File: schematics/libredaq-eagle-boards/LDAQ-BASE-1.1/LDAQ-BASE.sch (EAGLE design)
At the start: 90 parts, among them J1 4840.2211, J2 M50-3610542, T1 FDN340P, U1 ATSAM3U1CB, U2 LM3671MF-3.3, U3 TS30012-M050QFNR, U4 ISL3175, U5 LMV321, U6 TXB0108PWR, Y1 12M

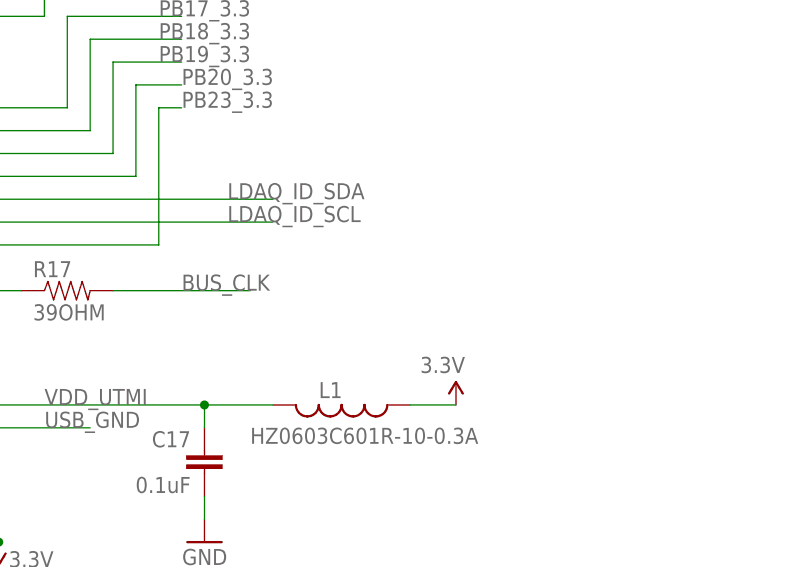
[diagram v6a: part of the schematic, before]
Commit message: Revision with CPLD (TODO: rewire)
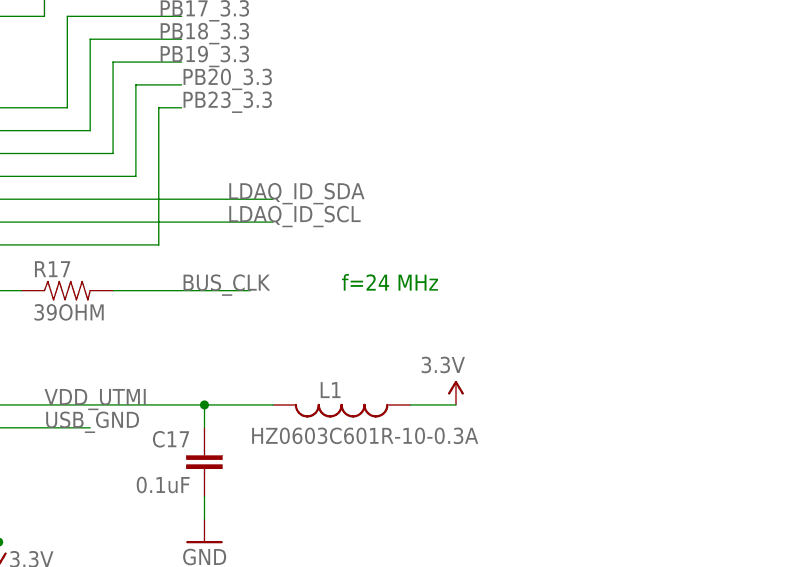
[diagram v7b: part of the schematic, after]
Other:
- note added: "f=24 MHz"
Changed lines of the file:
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@@
 <text x="381" y="406.4" size="1.778" layer="91">Amphenol ICC / FCI
 10018783-10201TLF</text>
+<text x="274.32" y="322.58" size="1.778" layer="91">f=24 MHz</text>
 </plain>
 <instances>
